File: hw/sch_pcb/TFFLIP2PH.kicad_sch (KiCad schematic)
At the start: 1 part, among them J1 Flipper_Zero

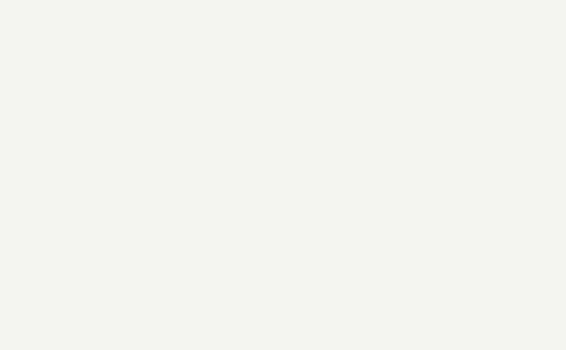
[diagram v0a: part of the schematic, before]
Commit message: Swap board sides to match top view on flipper zero.
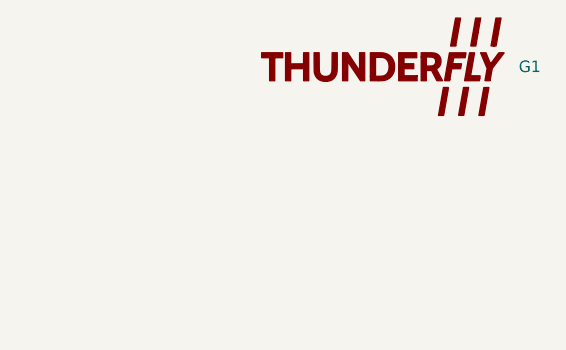
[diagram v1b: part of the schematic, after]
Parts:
- added G1: LOGO, TF_LOGA:TF 14x6,6, symbol TF_LOGO:LOGO
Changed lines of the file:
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@@
+	)
+	(symbol
+		(lib_id "TF_LOGO:LOGO")
+		(at 260.35 26.67 0)
+		(unit 1)
+		(exclude_from_sim no)
+		(in_bom no)
+		(on_board yes)
+		(dnp no)
+		(fields_autoplaced yes)
+		(property "Reference" "G1"
+			(at 275.59 26.6699 0)
+			(effects
+				(font
+					(size 1.27 1.27)
+				)
+				(justify left)
+			)
+		)
+		(property "Value" "LOGO"
+			(at 260.35 33.1376 0)
+			(effects
+				(font
+					(size 1.27 1.27)
+				)
+				(hide yes)
+			)
+		)
+		(property "Footprint" "TF_LOGA:TF 14x6,6"
+			(at 260.35 26.67 0)
+			(effects
+				(font
+					(size 1.27 1.27)
+				)
+				(hide yes)
+			)
+		)
+		(property "Datasheet" ""
+			(at 260.35 26.67 0)
+			(effects
+				(font
+					(size 1.27 1.27)
+				)
+				(hide yes)
+			)
+		)
+		(property "Description" ""
+			(at 260.35 26.67 0)
+			(effects
+				(font
+					(size 1.27 1.27)
+				)
+				(hide yes)
+			)
+		)
+		(property "UST_ID" ""
+			(at 260.35 26.67 0)
+			(effects
+				(font
+					(size 1.27 1.27)
+				)
+				(hide yes)
+			)
+		)
+		(instances
+			(project ""
+				(path "/c67f828b-18a5-4dea-9022-e222a7d410ef"
+					(reference "G1")
+					(unit 1)
+				)
+			)
+		)
 	)
 	(symbol

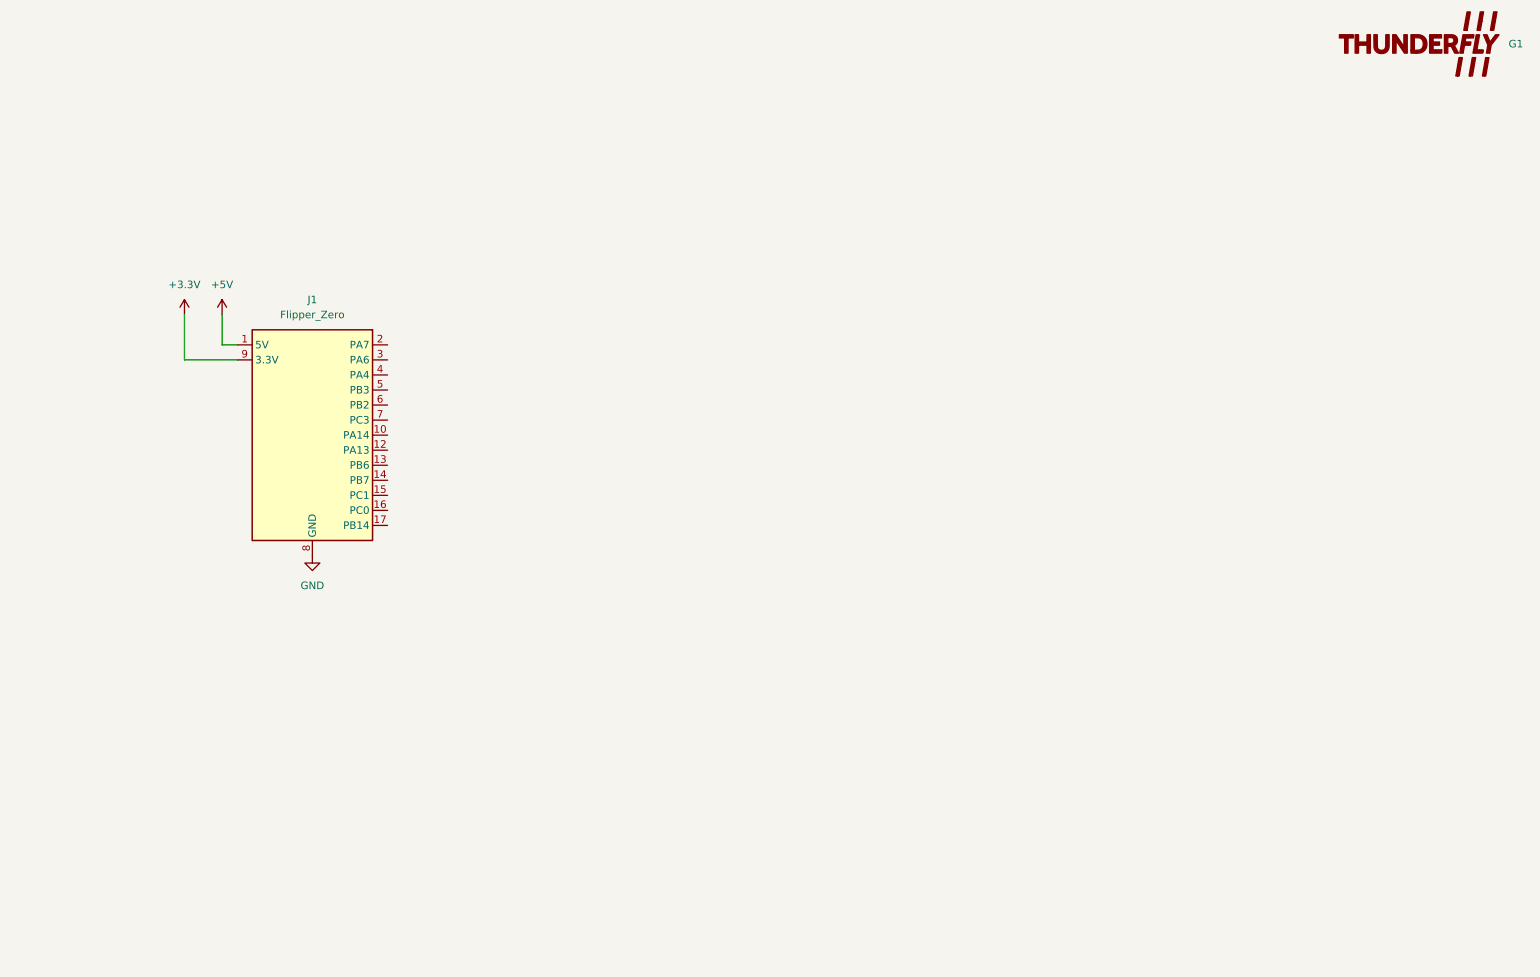
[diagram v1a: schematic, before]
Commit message: Initial set of connectors.
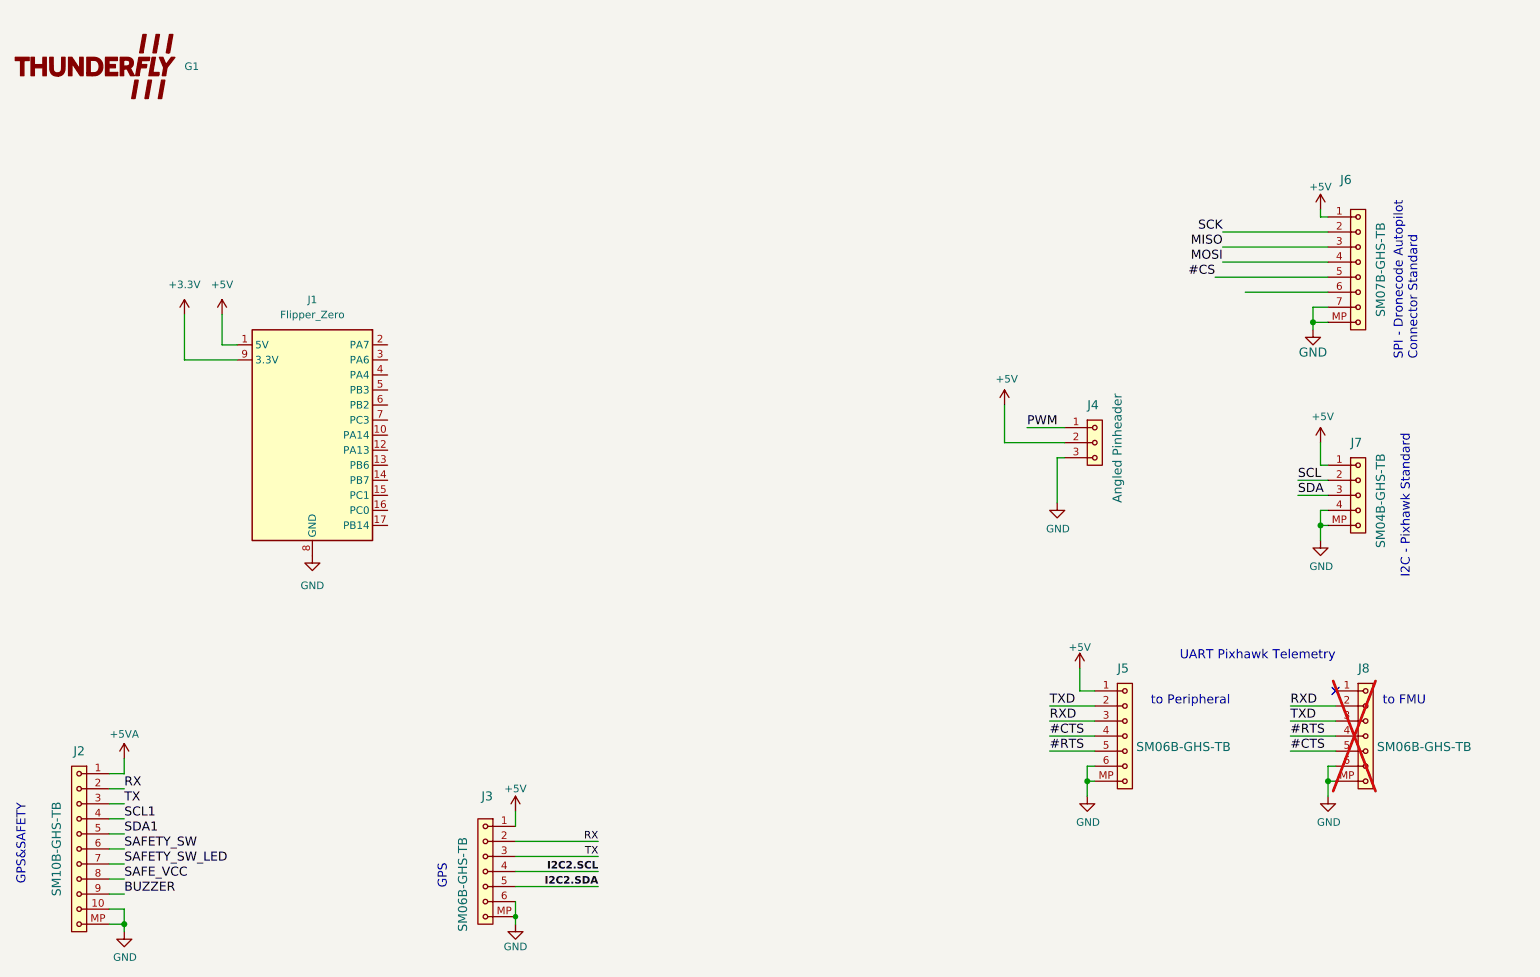
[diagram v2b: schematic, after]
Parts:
- added J2: SM10B-GHS-TB, Connector_JST:JST_GH_SM10B-GHS-TB_1x10-1MP_P1.25mm_Horizontal, symbol MLAB_CONNECTORS_JST:SM10B-GHS-TB
- added J3, J5, J8: SM06B-GHS-TB, Connector_JST:JST_GH_SM06B-GHS-TB_1x06-1MP_P1.25mm_Horizontal, symbol MLAB_CONNECTORS_JST:SM06B-GHS-TB
- added J4: Angled Pinheader, Connector_PinHeader_2.54mm:PinHeader_1x03_P2.54mm_Horizontal, symbol MLAB_HEADER:HEADER_1x03
- added J6: SM07B-GHS-TB, Connector_JST:JST_GH_SM07B-GHS-TB_1x07-1MP_P1.25mm_Horizontal, symbol ISM02A-rescue:SM07B-GHS-TB-MLAB_CONNECTORS_JST-ISM02A-rescue
- added J7: SM04B-GHS-TB, Connector_JST:JST_GH_SM04B-GHS-TB_1x04-1MP_P1.25mm_Horizontal, symbol MLAB_CONNECTORS_JST:SM04B-GHS-TB
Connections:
- net +5V: now also J3.1, J4.2, J5.1, J6.1, J7.1
- net GND: now also J2.10, J2.MP, J3.6, J3.MP, J4.3, J5.6, J5.MP, J6.7, J6.MP, J7.4, J7.MP, J8.6, J8.MP
- new net #CS: J6.5
- new net #CTS: J5.4, J8.5
- new net #RTS: J5.5, J8.4
- new net +5VA: J2.1
- new net BUZZER: J2.9
- new net I2C2.SCL: J3.4
- new net I2C2.SDA: J3.5
- new net MISO: J6.3
- new net MOSI: J6.4
- new net PWM: J4.1
- new net RX: J2.2, J3.2
- new net RXD: J5.3, J8.2
- new net SAFETY_SW: J2.6
- new net SAFETY_SW_LED: J2.7
- new net SAFE_VCC: J2.8
- new net SCK: J6.2
- new net SCL: J7.2
- new net SCL1: J2.4
- new net SDA: J7.3
- new net SDA1: J2.5
- new net TX: J2.3, J3.3
- new net TXD: J5.2, J8.3
- no-connect marks 0 -> 1
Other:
- note added: "GPS"
- note added: "GPS&SAFETY"
- note added: "I2C - Pixhawk Standard"
- note added: "SPI - Dronecode Autopilot Connector Standard"
- note added: "UART Pixhawk Telemetry"
- note added: "to FMU"
- note added: "to Peripheral"
- moved on the sheet: G1

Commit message: Routing in progress.
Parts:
- added J9: SM08B-GHS-TB, Connector_JST:JST_GH_SM08B-GHS-TB_1x08-1MP_P1.25mm_Horizontal, symbol MLAB_CONNECTORS_JST:SM08B-GHS-TB
- J6: symbol ISM02A-rescue:SM07B-GHS-TB-MLAB_CONNECTORS_JST-ISM02A-rescue -> MLAB_CONNECTORS_JST:SM07B-GHS-TB
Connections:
- net #CS is gone; now on net SS1: J6.5
- net +5VA is gone; now on net +5V: J2.1
- net I2C2.SCL is gone; now on net SCL: J3.4
- net I2C2.SDA is gone; now on net SDA: J3.5
- net MISO is gone; now on net #CTS: J6.3
- net PWM is gone; now on net MOSI: J4.1
- net RX is gone; now on net TXD: J2.2, J3.2
- net SAFETY_SW is gone; now on net GEO_STAT: J2.6
- net SAFETY_SW_LED is gone; now on net EXTINT: J2.7
- net SAFE_VCC is gone; now on net +3.3V: J2.8
- net SCK is gone; now on net #RTS: J6.2
- net SCL1 is gone; now on net SCL: J2.4
- net SDA1 is gone; now on net SDA: J2.5
- net TX is gone; now on net RXD: J2.3, J3.3
- net #CTS: now also J1.3 (PA6)
- net #RTS: now also J1.5 (PB3)
- net BUZZER: now also J1.17 (PB14)
- net GND: now also J9.8, J9.MP
- net MOSI: now also J1.2 (PA7)
- net RXD: now also J1.14 (PB7), J9.7
- net SCL: now also J1.16 (PC0), J9.5
- net SDA: now also J1.15 (PC1), J9.4
- net TXD: now also J1.13 (PB6), J9.6
- net TIMEPULSE: now reaches J1.10 (PA14)
- net TIMEPULSE: now also J9.1
- net EXTINT: now reaches J1.12 (PA13)
- net EXTINT: now also J9.2
- net SS1: now reaches J1.4 (PA4)
- net SS2: now reaches J1.6 (PB2)
- net SS2: now also J6.6
- net GEO_STAT: now reaches J1.7 (PC3)
- net GEO_STAT: now also J9.3
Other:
- note added: "Payload"
- moved on the sheet: J3, J4

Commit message: Improve layout and silkscreen.
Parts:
- G1: footprint TF_LOGA:TF 14x6,6 -> TF_LOGA:TF 10x4,7
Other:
- note added: "TF Payload"
- note removed: "Payload"
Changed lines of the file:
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@@
 		)
 	)
-	(text "Payload"
+	(text "TF Payload"
 		(exclude_from_sim no)
-		(at 128.27 154.94 90)
+		(at 128.27 153.67 90)
 		(effects
 			(font
@@
 			)
 		)
-		(property "Footprint" "TF_LOGA:TF 14x6,6"
+		(property "Footprint" "TF_LOGA:TF 10x4,7"
 			(at 36.83 30.48 0)
 			(effects

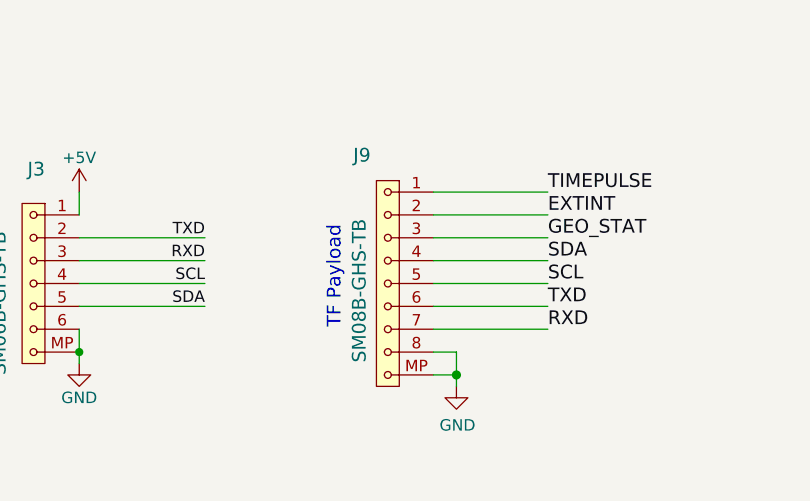
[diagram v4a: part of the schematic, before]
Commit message: Update silkscreen and manufacturing attributes.
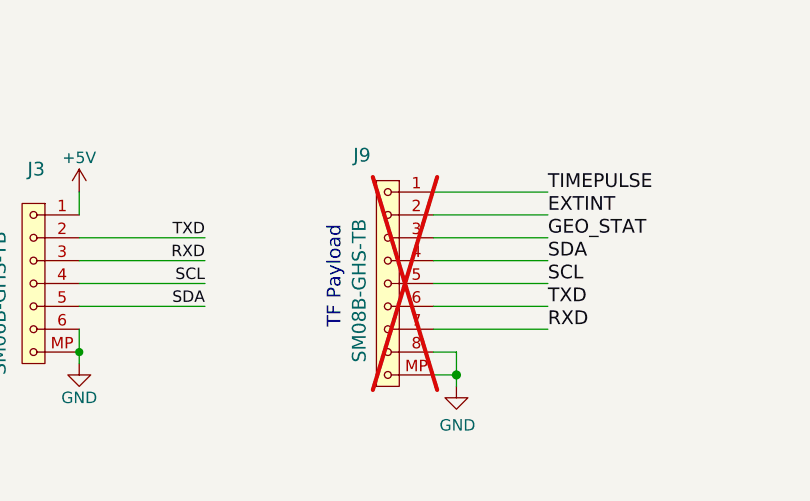
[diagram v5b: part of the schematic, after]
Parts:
- J3: UST_ID (none) -> 5fa0f70212875025b3977932
- J9: now not fitted
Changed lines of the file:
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@@
 		(in_bom yes)
 		(on_board yes)
-		(dnp no)
+		(dnp yes)
 		(property "Reference" "J9"
 			(at 131.4449 145.7681 0)
@@
 			(at 93.98 160.02 0)
 			(effects
+				(font
+					(size 1.27 1.27)
+				)
+				(hide yes)
+			)
+		)
+		(property "UST_ID" "5fa0f70212875025b3977932"
+			(at 93.98 160.02 0)
+			(effects
